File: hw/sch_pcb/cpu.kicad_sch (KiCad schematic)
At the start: 24 parts, among them J19 HEADER_2x01_PARALLEL, J22 HEADER_2x03, J4 HEADER_1x01, J5 HEADER_1x01, J6 HEADER_1x01, J7 HEADER_1x01, U10 ATMEGA1284P-AU, U11 PCF85263A, Y2 ABS07-120-32.768KHZ-T

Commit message: update ustid
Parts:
- C26, C27, C28, C31, C34, C35, C39, C44, C47: UST_ID (none) -> 5c70984712875079b91f8b4c
- C40: UST_ID (none) -> 5c70984712875079b91f8b53
- C43: UST_ID (none) -> 5e3ff8fc1287502a33bad7a3
- J19, J22, J4, J5, J6, J7: now left out of the parts list
- L1: UST_ID (none) -> 5c70984412875079b91f87ff
- R20, R21, R23: UST_ID (none) -> 5c70984612875079b91f899f
- U10: UST_ID (none) -> 5c70984712875079b91f8b5b
- U11: UST_ID (none) -> 5c70984612875079b91f8a0c
- Y2: UST_ID (none) -> 5c70984712875079b91f8b1b

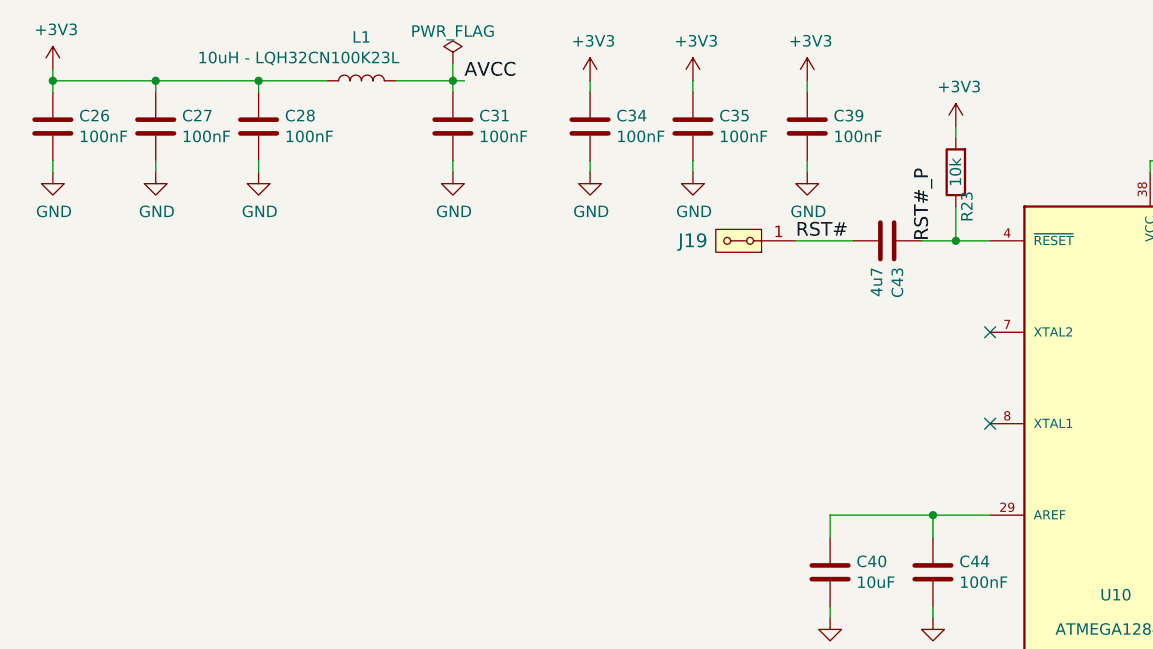
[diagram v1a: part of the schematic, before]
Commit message: Update titleblock to fix schematics PDF generation. Improve schematics layout.
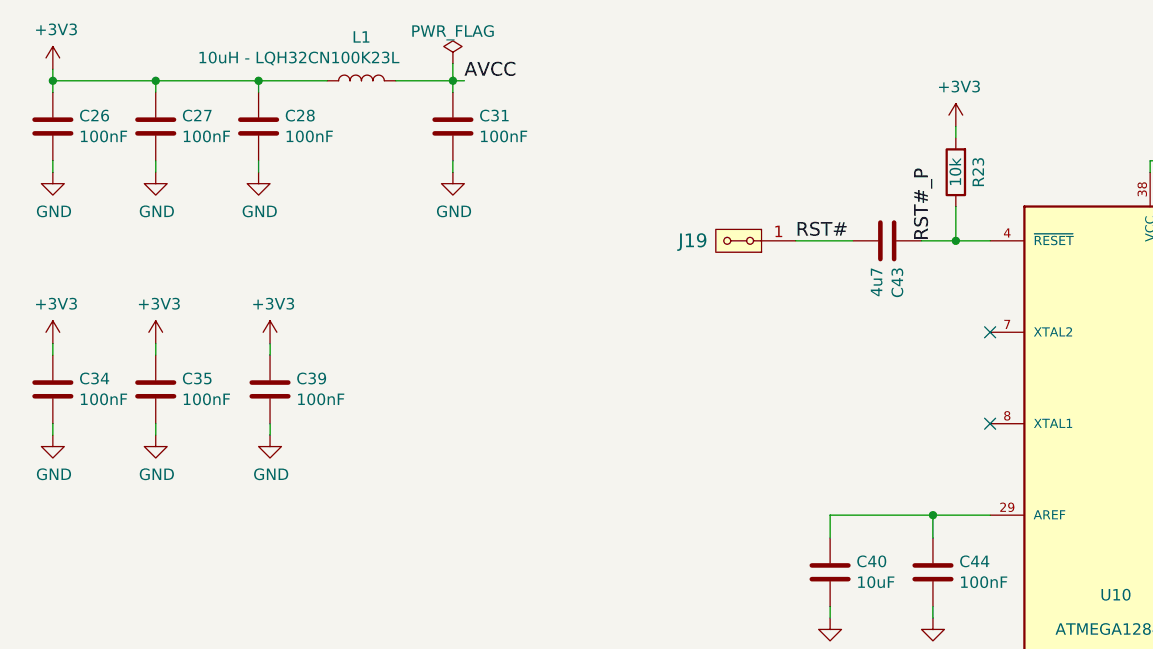
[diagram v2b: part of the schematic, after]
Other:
- moved on the sheet: C34, C35, C39
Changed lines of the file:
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@@
 	(wire
 		(pts
-			(xy 90.17 20.32) (xy 90.17 21.59)
+			(xy 30.48 49.53) (xy 30.48 50.8)
 		)
 		(stroke
@@
 	(wire
 		(pts
-			(xy 102.87 20.32) (xy 102.87 21.59)
+			(xy 43.18 49.53) (xy 43.18 50.8)
 		)
 		(stroke
@@
 	(wire
 		(pts
-			(xy 78.74 30.48) (xy 78.74 29.21)
+			(xy 19.05 59.69) (xy 19.05 58.42)
 		)
 		(stroke
@@
 	(wire
 		(pts
-			(xy 78.74 20.32) (xy 78.74 21.59)
+			(xy 19.05 49.53) (xy 19.05 50.8)
 		)
 		(stroke
@@
 	(wire
 		(pts
-			(xy 90.17 30.48) (xy 90.17 29.21)
+			(xy 30.48 59.69) (xy 30.48 58.42)
 		)
 		(stroke
@@
 	(wire
 		(pts
-			(xy 102.87 30.48) (xy 102.87 29.21)
+			(xy 43.18 59.69) (xy 43.18 58.42)
 		)
 		(stroke
@@
 		(dnp no)
 		(property "Reference" "R23"
-			(at 120.65 34.29 90)
+			(at 121.92 30.48 90)
 			(effects
 				(font
@@
 	(symbol
 		(lib_id "SPACEDOS01B_PCB01A-rescue:C-device-DATALOGGER01A-rescue-CCP2019V01A-rescue-SPACEDOS01A_PCB01A-rescue")
-		(at 78.74 25.4 0)
+		(at 19.05 54.61 0)
 		(unit 1)
 		(exclude_from_sim no)
@@
 		(dnp no)
 		(property "Reference" "C34"
-			(at 81.661 24.2316 0)
+			(at 21.971 53.4416 0)
 			(effects
 				(font
@@
 		)
 		(property "Value" "100nF"
-			(at 81.661 26.543 0)
+			(at 21.971 55.753 0)
 			(effects
 				(font
@@
 		)
 		(property "Footprint" "Mlab_R:SMD-0805"
-			(at 79.7052 29.21 0)
+			(at 20.0152 58.42 0)
 			(effects
 				(font
@@
 		)
 		(property "Datasheet" ""
-			(at 78.74 25.4 0)
+			(at 19.05 54.61 0)
 			(effects
 				(font
@@
 		)
 		(property "Description" ""
-			(at 78.74 25.4 0)
+			(at 19.05 54.61 0)
 			(effects
 				(font
@@
 		)
 		(property "UST_ID" "5c70984712875079b91f8b4c"
-			(at 78.74 25.4 0)
+			(at 19.05 54.61 0)
 			(effects
 				(font
@@
 	(symbol
 		(lib_id "power:GND")
-		(at 78.74 30.48 0)
+		(at 19.05 59.69 0)
 		(unit 1)
 		(exclude_from_sim no)
@@
 		(dnp no)
 		(property "Reference" "#PWR0154"
-			(at 78.74 36.83 0)
+			(at 19.05 66.04 0)
 			(effects
 				(font
@@
 		)
 		(property "Value" "GND"
-			(at 78.867 34.8742 0)
+			(at 19.177 64.0842 0)
 			(effects
 				(font
@@
 		)
 		(property "Footprint" ""
-			(at 78.74 30.48 0)
+			(at 19.05 59.69 0)
 			(effects
 				(font
@@
 		)
 		(property "Datasheet" ""
-			(at 78.74 30.48 0)
+			(at 19.05 59.69 0)
 			(effects
 				(font
@@
 		)
 		(property "Description" ""
-			(at 78.74 30.48 0)
+			(at 19.05 59.69 0)
 			(effects
 				(font
@@
 	(symbol
 		(lib_id "SPACEDOS01B_PCB01A-rescue:C-device-DATALOGGER01A-rescue-CCP2019V01A-rescue-SPACEDOS01A_PCB01A-rescue")
-		(at 90.17 25.4 0)
+		(at 30.48 54.61 0)
 		(unit 1)
 		(exclude_from_sim no)
@@
 		(dnp no)
 		(property "Reference" "C35"
-			(at 93.091 24.2316 0)
+			(at 33.401 53.4416 0)
 			(effects
 				(font
@@
 		)
 		(property "Value" "100nF"
-			(at 93.091 26.543 0)
+			(at 33.401 55.753 0)
 			(effects
 				(font
@@
 		)
 		(property "Footprint" "Mlab_R:SMD-0805"
-			(at 91.1352 29.21 0)
+			(at 31.4452 58.42 0)
 			(effects
 				(font
@@
 		)
 		(property "Datasheet" ""
-			(at 90.17 25.4 0)
+			(at 30.48 54.61 0)
 			(effects
 				(font
@@
 		)
 		(property "Description" ""
-			(at 90.17 25.4 0)
+			(at 30.48 54.61 0)
 			(effects
 				(font
@@
 		)
 		(property "UST_ID" "5c70984712875079b91f8b4c"
-			(at 90.17 25.4 0)
+			(at 30.48 54.61 0)
 			(effects
 				(font
@@
 	(symbol
 		(lib_id "power:GND")
-		(at 90.17 30.48 0)
+		(at 30.48 59.69 0)
 		(unit 1)
 		(exclude_from_sim no)
@@
 		(dnp no)
 		(property "Reference" "#PWR0156"
-			(at 90.17 36.83 0)
+			(at 30.48 66.04 0)
 			(effects
 				(font
@@
 		)
 		(property "Value" "GND"
-			(at 90.297 34.8742 0)
+			(at 30.607 64.0842 0)
 			(effects
 				(font
@@
 		)
 		(property "Footprint" ""
-			(at 90.17 30.48 0)
+			(at 30.48 59.69 0)
 			(effects
 				(font
@@
 		)
 		(property "Datasheet" ""
-			(at 90.17 30.48 0)
+			(at 30.48 59.69 0)
 			(effects
 				(font
@@
 		)
 		(property "Description" ""
-			(at 90.17 30.48 0)
+			(at 30.48 59.69 0)
 			(effects
 				(font
@@
 	(symbol
 		(lib_id "SPACEDOS01B_PCB01A-rescue:C-device-DATALOGGER01A-rescue-CCP2019V01A-rescue-SPACEDOS01A_PCB01A-rescue")
-		(at 102.87 25.4 0)
+		(at 43.18 54.61 0)
 		(unit 1)
 		(exclude_from_sim no)
@@
 		(dnp no)
 		(property "Reference" "C39"
-			(at 105.791 24.2316 0)
+			(at 46.101 53.4416 0)
 			(effects
 				(font
@@
 		)
 		(property "Value" "100nF"
-			(at 105.791 26.543 0)
+			(at 46.101 55.753 0)
 			(effects
 				(font
@@
 		)
 		(property "Footprint" "Mlab_R:SMD-0805"
-			(at 103.8352 29.21 0)
+			(at 44.1452 58.42 0)
 			(effects
 				(font
@@
 		)
 		(property "Datasheet" ""
-			(at 102.87 25.4 0)
+			(at 43.18 54.61 0)
 			(effects
 				(font
@@
 		)
 		(property "Description" ""
-			(at 102.87 25.4 0)
+			(at 43.18 54.61 0)
 			(effects
 				(font
@@
 		)
 		(property "UST_ID" "5c70984712875079b91f8b4c"
-			(at 102.87 25.4 0)
+			(at 43.18 54.61 0)
 			(effects
 				(font
@@
 	(symbol
 		(lib_id "power:GND")
-		(at 102.87 30.48 0)
+		(at 43.18 59.69 0)
 		(unit 1)
 		(exclude_from_sim no)
@@
 		(dnp no)
 		(property "Reference" "#PWR0158"
-			(at 102.87 36.83 0)
+			(at 43.18 66.04 0)
 			(effects
 				(font
@@
 		)
 		(property "Value" "GND"
-			(at 102.997 34.8742 0)
+			(at 43.307 64.0842 0)
 			(effects
 				(font
@@
 		)
 		(property "Footprint" ""
-			(at 102.87 30.48 0)
+			(at 43.18 59.69 0)
 			(effects
 				(font
@@
 		)
 		(property "Datasheet" ""
-			(at 102.87 30.48 0)
+			(at 43.18 59.69 0)
 			(effects
 				(font
@@
 		)
 		(property "Description" ""
-			(at 102.87 30.48 0)
+			(at 43.18 59.69 0)
 			(effects
 				(font
@@
 	(symbol
 		(lib_id "power:+3.3V")
-		(at 78.74 20.32 0)
+		(at 19.05 49.53 0)
 		(unit 1)
 		(exclude_from_sim no)
@@
 		(dnp no)
 		(property "Reference" "#PWR0120"
-			(at 78.74 24.13 0)
+			(at 19.05 53.34 0)
 			(effects
 				(font
@@
 		)
 		(property "Value" "+3V3"
-			(at 79.121 15.9258 0)
+			(at 19.431 45.1358 0)
 			(effects
 				(font
@@
 		)
 		(property "Footprint" ""
-			(at 78.74 20.32 0)
+			(at 19.05 49.53 0)
 			(effects
 				(font
@@
 		)
 		(property "Datasheet" ""
-			(at 78.74 20.32 0)
+			(at 19.05 49.53 0)
 			(effects
 				(font
@@
 		)
 		(property "Description" ""
-			(at 78.74 20.32 0)
+			(at 19.05 49.53 0)
 			(effects
 				(font
@@
 	(symbol
 		(lib_id "power:+3.3V")
-		(at 90.17 20.32 0)
+		(at 30.48 49.53 0)
 		(unit 1)
 		(exclude_from_sim no)
@@
 		(dnp no)
 		(property "Reference" "#PWR0130"
-			(at 90.17 24.13 0)
+			(at 30.48 53.34 0)
 			(effects
 				(font
@@
 		)
 		(property "Value" "+3V3"
-			(at 90.551 15.9258 0)
+			(at 30.861 45.1358 0)
 			(effects
 				(font
@@
 		)
 		(property "Footprint" ""
-			(at 90.17 20.32 0)
+			(at 30.48 49.53 0)
 			(effects
 				(font
@@
 		)
 		(property "Datasheet" ""
-			(at 90.17 20.32 0)
+			(at 30.48 49.53 0)
 			(effects
 				(font
@@
 		)
 		(property "Description" ""
-			(at 90.17 20.32 0)
+			(at 30.48 49.53 0)
 			(effects
 				(font
@@
 	(symbol
 		(lib_id "power:+3.3V")
-		(at 102.87 20.32 0)
+		(at 43.18 49.53 0)
 		(unit 1)
 		(exclude_from_sim no)
@@
 		(dnp no)
 		(property "Reference" "#PWR0131"
-			(at 102.87 24.13 0)
+			(at 43.18 53.34 0)
 			(effects
 				(font
@@
 		)
 		(property "Value" "+3V3"
-			(at 103.251 15.9258 0)
+			(at 43.561 45.1358 0)
 			(effects
 				(font
@@
 		)
 		(property "Footprint" ""
-			(at 102.87 20.32 0)
+			(at 43.18 49.53 0)
 			(effects
 				(font
@@
 		)
 		(property "Datasheet" ""
-			(at 102.87 20.32 0)
+			(at 43.18 49.53 0)
 			(effects
 				(font
@@
 		)
 		(property "Description" ""
-			(at 102.87 20.32 0)
+			(at 43.18 49.53 0)
 			(effects
 				(font
